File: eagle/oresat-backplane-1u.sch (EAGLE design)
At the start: 35 parts

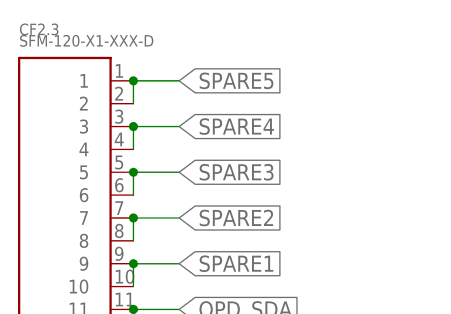
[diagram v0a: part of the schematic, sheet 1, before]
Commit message: TNAMES cleanup, renamed by card number.
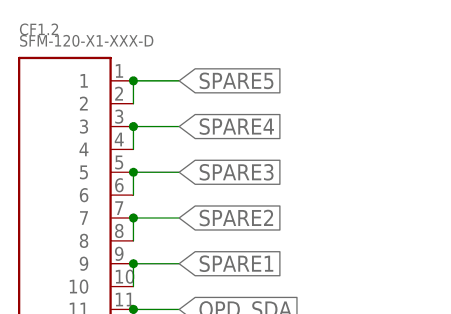
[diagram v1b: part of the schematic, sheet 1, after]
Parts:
- renumbered CF2.3 to CF1.2, CM2.4 to CM3.2, CM2.5 to CM4.1

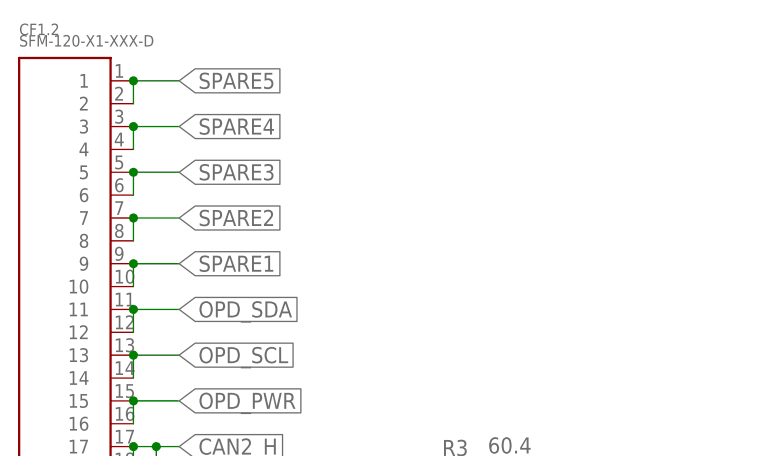
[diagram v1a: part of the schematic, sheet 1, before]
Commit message: Added 1U -Z end cap connector.
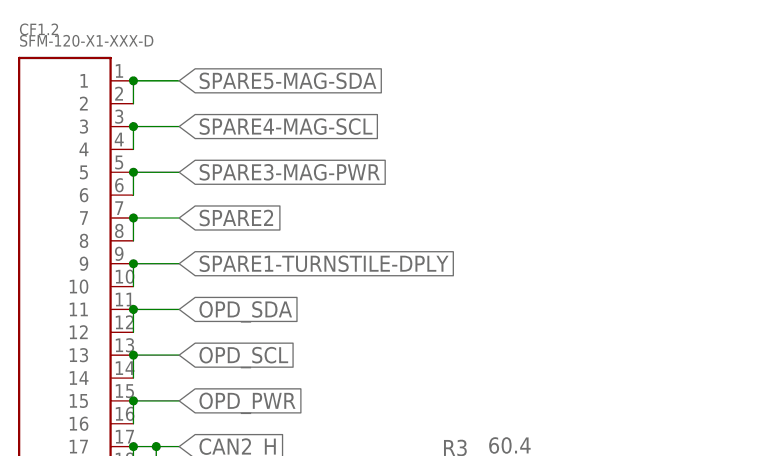
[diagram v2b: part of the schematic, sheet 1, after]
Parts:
- added J1: 5-104196-5, J-TE-5-104196-5-RA-1.27mm-female-th:5-104196-5
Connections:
- removed net SPARE1: CF1.2.10, CF1.2.9, CF2.2.10, CF2.2.9, CF3.2.10, CF3.2.9, CF4.2.10, CF4.2.9, CF5.2.10, CF5.2.9, CF6.2.10, CF6.2.9, CF7.2.10, CF7.2.9, CF8.2.10, CF8.2.9
- removed net SPARE3: CF1.2.5, CF1.2.6, CF2.2.5, CF2.2.6, CF3.2.5, CF3.2.6, CF4.2.5, CF4.2.6, CF5.2.5, CF5.2.6, CF6.2.5, CF6.2.6, CF7.2.5, CF7.2.6, CF8.2.5, CF8.2.6
- removed net SPARE4: CF1.2.3, CF1.2.4, CF2.2.3, CF2.2.4, CF3.2.3, CF3.2.4, CF4.2.3, CF4.2.4, CF5.2.3, CF5.2.4, CF6.2.3, CF6.2.4, CF7.2.3, CF7.2.4, CF8.2.3, CF8.2.4
- removed net SPARE5: CF1.2.1, CF1.2.2, CF2.2.1, CF2.2.2, CF3.2.1, CF3.2.2, CF4.2.1, CF4.2.2, CF5.2.1, CF5.2.2, CF6.2.1, CF6.2.2, CF7.2.1, CF7.2.2, CF8.2.1, CF8.2.2
- new net SPARE1-TURNSTILE-DPLY: CF1.2.10, CF1.2.9, CF2.2.10, CF2.2.9, CF3.2.10, CF3.2.9, CF4.2.10, CF4.2.9, CF5.2.10, CF5.2.9, CF6.2.10, CF6.2.9, CF7.2.10, CF7.2.9, CF8.2.10, CF8.2.9, J1.13
- new net SPARE3-MAG-PWR: CF1.2.5, CF1.2.6, CF2.2.5, CF2.2.6, CF3.2.5, CF3.2.6, CF4.2.5, CF4.2.6, CF5.2.5, CF5.2.6, CF6.2.5, CF6.2.6, CF7.2.5, CF7.2.6, CF8.2.5, CF8.2.6, J1.15, J1.16
- new net SPARE4-MAG-SCL: CF1.2.3, CF1.2.4, CF2.2.3, CF2.2.4, CF3.2.3, CF3.2.4, CF4.2.3, CF4.2.4, CF5.2.3, CF5.2.4, CF6.2.3, CF6.2.4, CF7.2.3, CF7.2.4, CF8.2.3, CF8.2.4, J1.17, J1.18
- new net SPARE5-MAG-SDA: CF1.2.1, CF1.2.2, CF2.2.1, CF2.2.2, CF3.2.1, CF3.2.2, CF4.2.1, CF4.2.2, CF5.2.1, CF5.2.2, CF6.2.1, CF6.2.2, CF7.2.1, CF7.2.2, CF8.2.1, CF8.2.2, J1.19, J1.20
- net !SD: now also J1.1
- net CAN1_H: now also J1.4
- net CAN1_L: now also J1.3
- net CAN2_H: now also J1.9
- net CAN2_L: now also J1.8
- net GND: now also J1.2, J1.5, J1.6, J1.HD
- net OPD_PWR: now also J1.10
- net OPD_SCL: now also J1.11
- net OPD_SDA: now also J1.12
- net SPARE2: now also J1.14
- net VBUS: now also J1.7

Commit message: Backplane v1.1!
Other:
- note added: "-Z End Cap Connector"
- note added: "v1.1"
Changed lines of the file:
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@@
 <setting verticaltext="up"/>
 </settings>
-<grid distance="0.05" unitdist="inch" unit="inch" style="lines" multiple="1" display="no" altdistance="0.01" altunitdist="inch" altunit="inch"/>
+<grid distance="0.1" unitdist="inch" unit="inch" style="lines" multiple="1" display="no" altdistance="0.01" altunitdist="inch" altunit="inch"/>
 <layers>
 <layer number="1" name="Top" color="4" fill="1" visible="no" active="no"/>
@@
 <part name="J1" library="J-TE-5-104196-5-RA-1.27mm-female-th" deviceset="5-104196-5" device=""/>
 <part name="GND6" library="supply" deviceset="GND" device=""/>
-<part name="GND7" library="supply" deviceset="GND" device=""/>
 </parts>
 <sheets>
@@
 <description>Slot 1</description>
 <plain>
+<text x="264.16" y="7.62" size="2.54" layer="97">v1.1</text>
 </plain>
 <instances>
@@
 <description>To -Z End Cap</description>
 <plain>
+<text x="91.44" y="88.9" size="2.54" layer="97">-Z End Cap Connector</text>
 </plain>
 <instances>
@@
 </instance>
 <instance part="GND6" gate="G1" x="104.14" y="97.79" smashed="yes"/>
-<instance part="GND7" gate="G1" x="132.08" y="185.42" smashed="yes"/>
 </instances>
 <busses>
@@
 <net name="GND" class="0">
 <segment>
-<pinref part="GND7" gate="G1" pin="GND"/>
-<wire x1="132.08" y1="185.42" x2="132.08" y2="187.96" width="0.1524" layer="91"/>
-</segment>
-<segment>
 <pinref part="J1" gate="G$1" pin="HD"/>

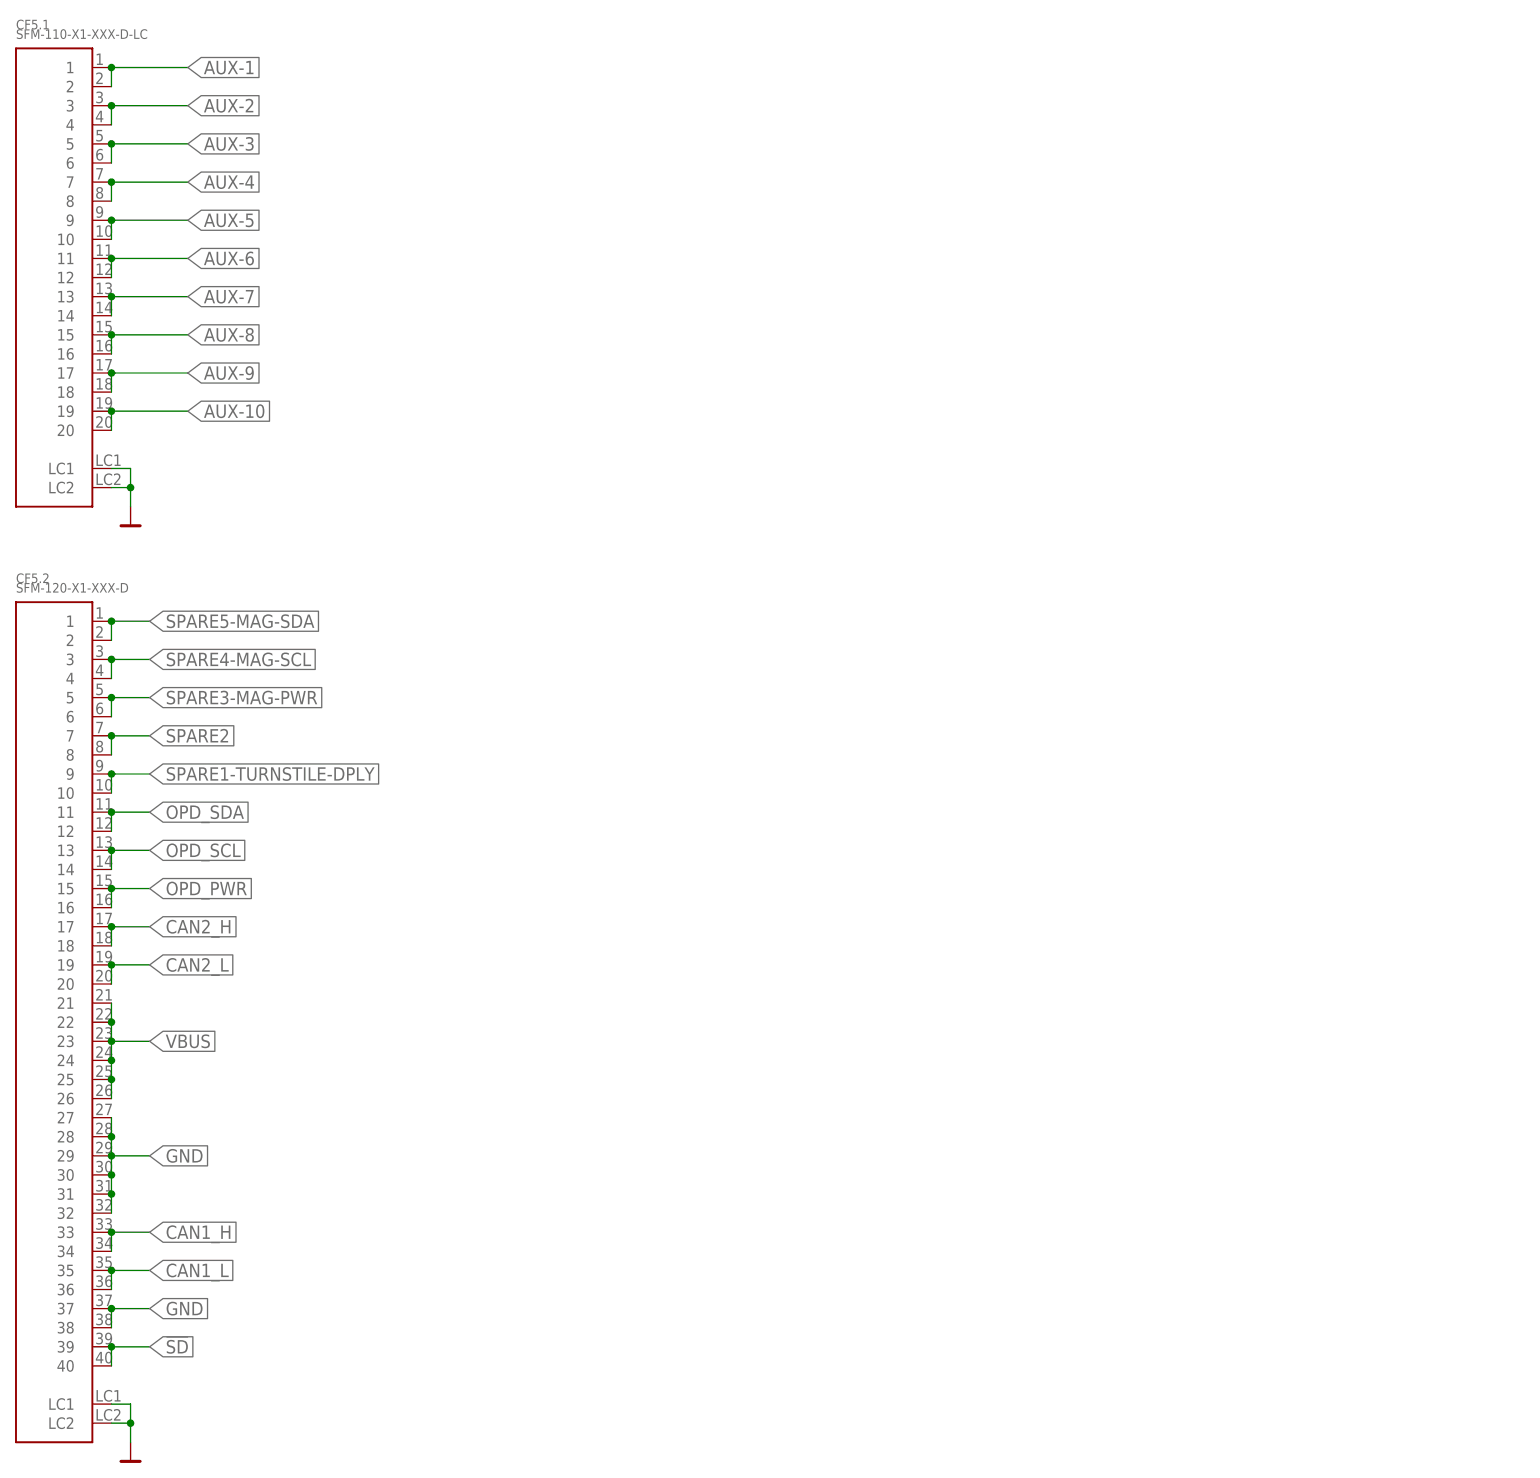
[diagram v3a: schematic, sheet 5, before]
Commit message: Updated 1U backplane to v1.2. Better position of end cap connector, added debug connector.
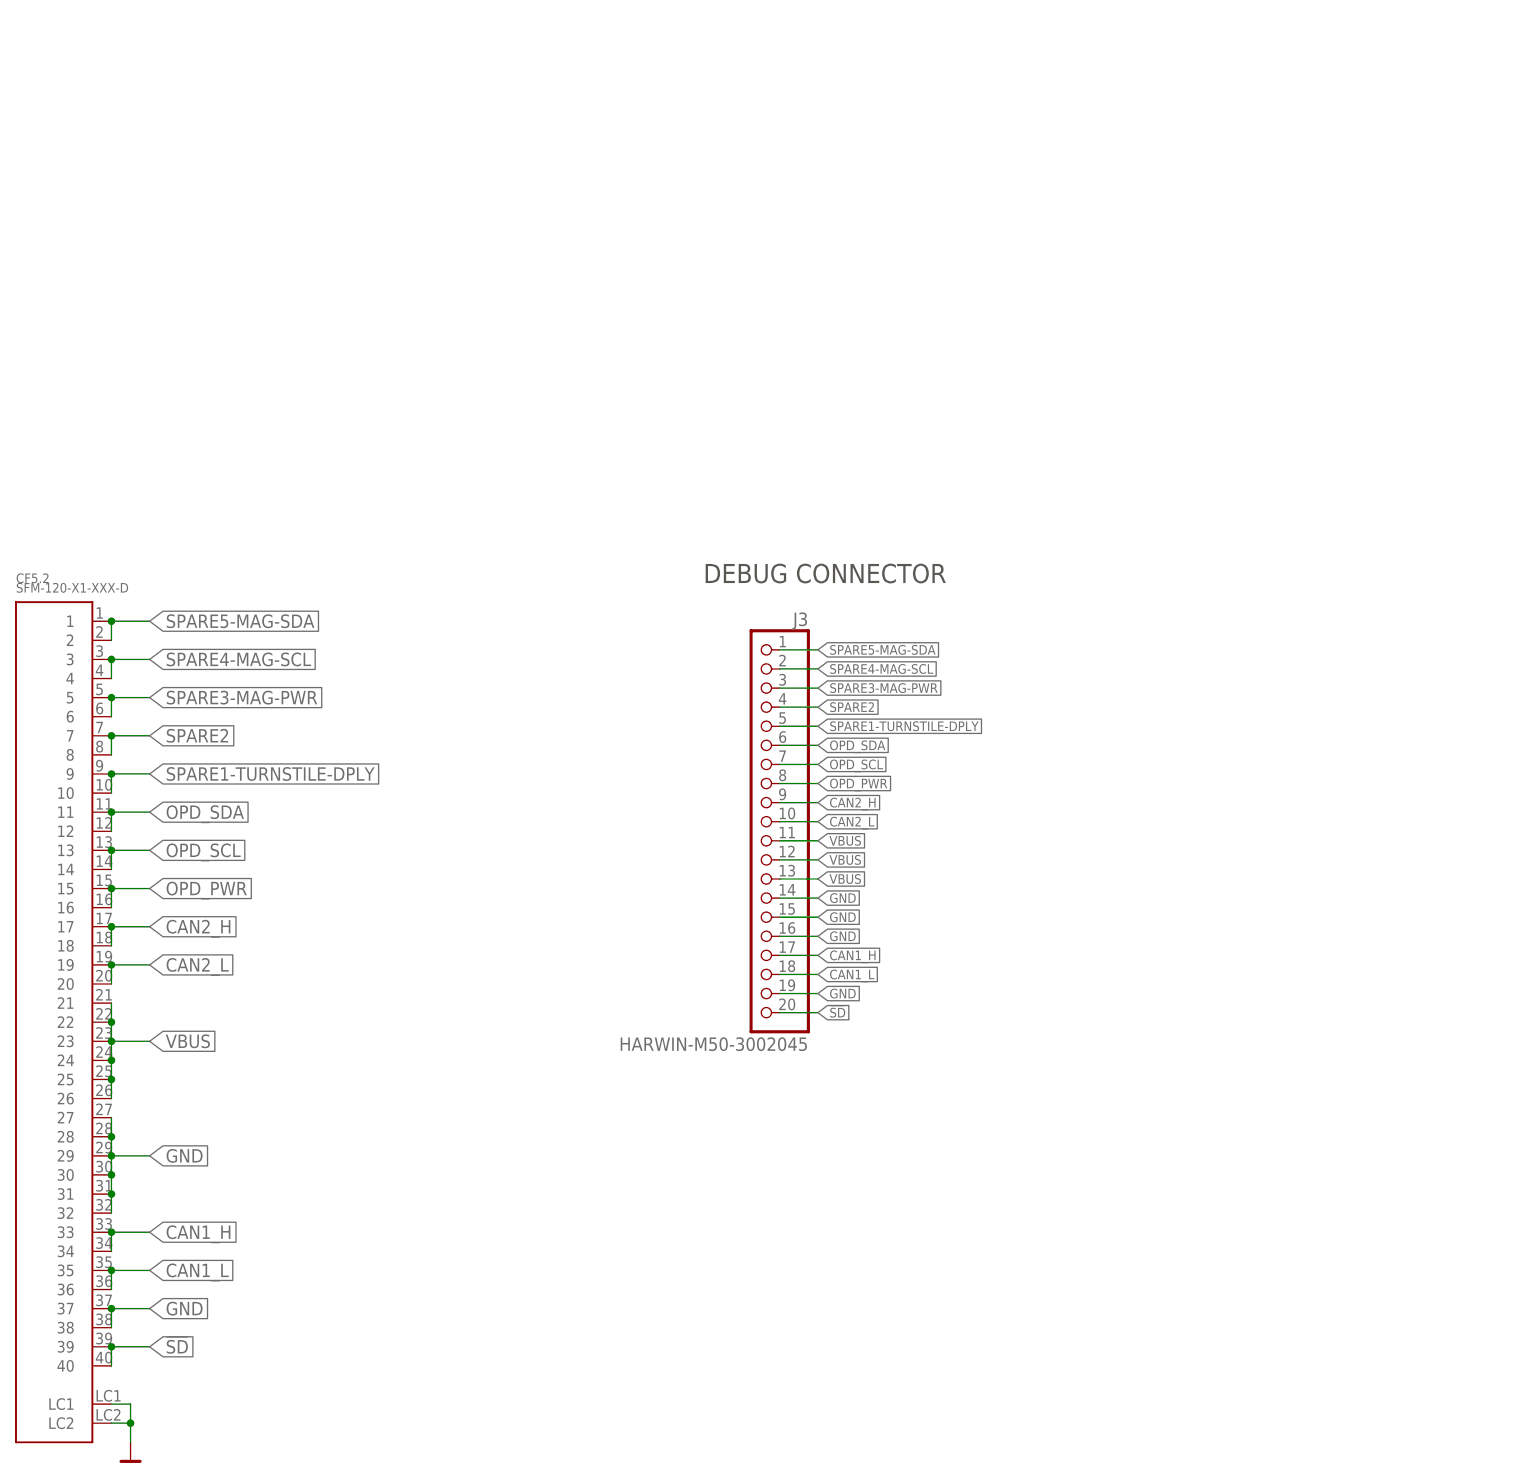
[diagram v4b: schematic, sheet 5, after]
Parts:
- removed CF5.1, CF6.1: SFM-110-X1-XXX-D-LC, J-Samtec-SFM-110-X1-XXX-D-LC:SFM-110-X1-XXX-D-LC
- added J3: HARWIN-M50-3002045, J-Harwin-M50-3002045-20pin-1.27-F-vertical:HARWIN-M50-3002045
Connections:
- net !SD: now also J3.20; no longer J1.1
- net AUX-1: no longer CF5.1.1, CF5.1.2, CF6.1.1, CF6.1.2
- net AUX-10: no longer CF5.1.19, CF5.1.20, CF6.1.19, CF6.1.20
- net AUX-2: no longer CF5.1.3, CF5.1.4, CF6.1.3, CF6.1.4
- net AUX-3: no longer CF5.1.5, CF5.1.6, CF6.1.5, CF6.1.6
- net AUX-4: no longer CF5.1.7, CF5.1.8, CF6.1.7, CF6.1.8
- net AUX-5: no longer CF5.1.10, CF5.1.9, CF6.1.10, CF6.1.9
- net AUX-6: no longer CF5.1.11, CF5.1.12, CF6.1.11, CF6.1.12
- net AUX-7: no longer CF5.1.13, CF5.1.14, CF6.1.13, CF6.1.14
- net AUX-8: no longer CF5.1.15, CF5.1.16, CF6.1.15, CF6.1.16
- net AUX-9: no longer CF5.1.17, CF5.1.18, CF6.1.17, CF6.1.18
- net CAN1_H: now also J3.17; no longer J1.4
- net CAN1_L: now also J3.18; no longer J1.3
- net CAN2_H: now also J3.9; no longer J1.9
- net CAN2_L: now also J3.10; no longer J1.8
- net GND: now also J1.1, J1.10, J1.11, J1.12, J1.3, J1.4, J1.7, J1.8, J1.9, J3.14, J3.15, J3.16, J3.19; no longer CF5.1.LC1, CF5.1.LC2, CF6.1.LC1, CF6.1.LC2
- net OPD_PWR: now also J3.8; no longer J1.10
- net OPD_SCL: now also J3.7; no longer J1.11
- net OPD_SDA: now also J3.6; no longer J1.12
- net SPARE1-TURNSTILE-DPLY: now also J3.5; no longer J1.13
- net SPARE2: now also J1.13, J3.4
- net SPARE3-MAG-PWR: now also J3.3
- net SPARE4-MAG-SCL: now also J3.2
- net SPARE5-MAG-SDA: now also J3.1
- net VBUS: now also J3.11, J3.12, J3.13; no longer J1.7
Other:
- note added: "DEBUG CONNECTOR"

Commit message: Final tweaks to v1.2 - off to fab.
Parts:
- added U$1: FLIGHMARKERNEW, oresat-flight-marker:FLIGHMARKERNEW
- J3: device J-Harwin-M50-3002045-20pin-1.27-F-vertical:HARWIN-M50-3002045 -> J-Harwin-M50-3002045-20pin-1.27-F-and-M-vertical-th:HARWIN-M50-3002045
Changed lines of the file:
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@@
 <setting verticaltext="up"/>
 </settings>
-<grid distance="0.05" unitdist="inch" unit="inch" style="lines" multiple="2" display="no" altdistance="0.01" altunitdist="inch" altunit="inch"/>
+<grid distance="0.1" unitdist="inch" unit="inch" style="lines" multiple="1" display="no" altdistance="0.01" altunitdist="inch" altunit="inch"/>
 <layers>
 <layer number="1" name="Top" color="4" fill="1" visible="no" active="no"/>
@@
 <part name="J1" library="J-TE-5-104196-5-RA-1.27mm-female-th" deviceset="5-104196-5" device=""/>
 <part name="GND6" library="supply" deviceset="GND" device=""/>
-<part name="J3" library="J-Harwin-M50-3002045-20pin-1.27-F-vertical" deviceset="HARWIN-M50-3002045" device=""/>
+<part name="J3" library="J-Harwin-M50-3002045-20pin-1.27-F-and-M-vertical-th" deviceset="HARWIN-M50-3002045" device=""/>
 <part name="GND7" library="supply" deviceset="GND" device=""/>
+<part name="U$1" library="oresat-flight-marker" deviceset="FLIGHMARKER" device="NEW"/>
 </parts>
 <sheets>
@@
 <instance part="GND2" gate="G1" x="147.32" y="83.82" smashed="yes"/>
 <instance part="GND3" gate="G1" x="147.32" y="68.58" smashed="yes"/>
+<instance part="U$1" gate="G$1" x="121.92" y="2.54" smashed="yes"/>
 </instances>
 <busses>
